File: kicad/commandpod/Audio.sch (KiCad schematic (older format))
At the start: 10 parts

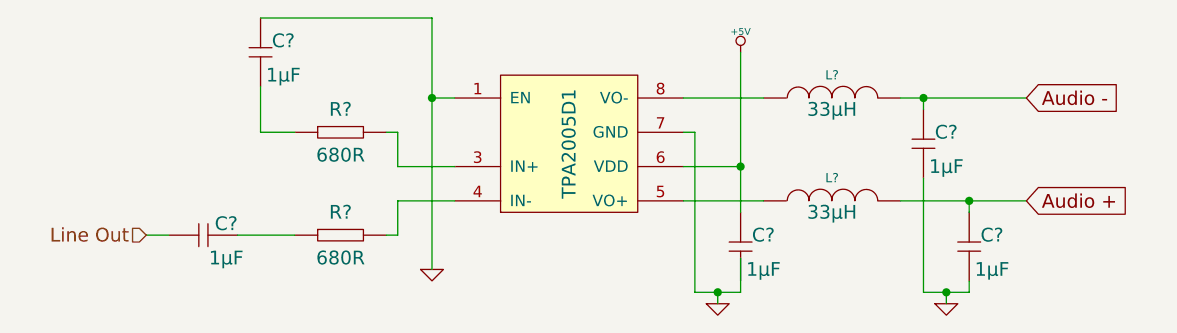
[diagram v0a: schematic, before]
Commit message: Annotated schematics
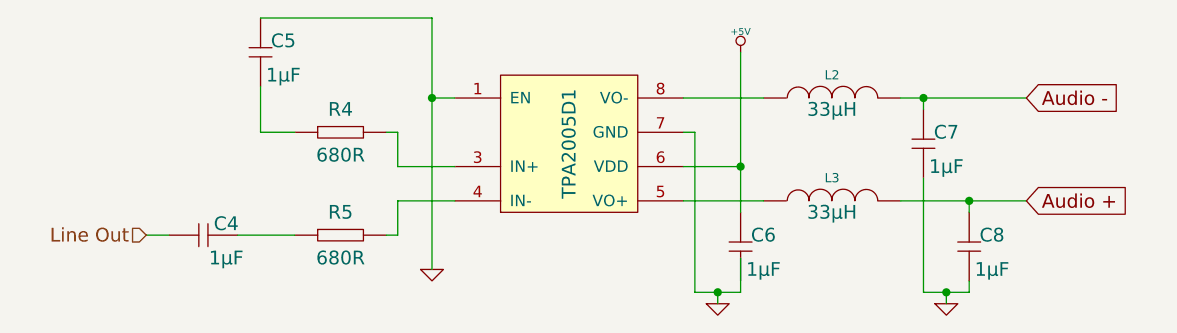
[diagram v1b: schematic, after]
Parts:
- gave numbers to parts that had none: 10
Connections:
- wire segments 36 -> 30
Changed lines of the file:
@@
 $EndDescr
 $Comp
-L TPA2005D1 AMP?
+L TPA2005D1 AMP1
 U 1 1 56D7C1D5
 P 5300 3600
-F 0 "AMP?" H 5100 3250 60  0001 C CNN
+F 0 "AMP1" H 5100 3250 60  0001 C CNN
 F 1 "TPA2005D1" V 5300 3600 60  0000 C CNN
 F 2 "" H 5250 3550 60  0000 C CNN
@@
 Audio -
 $Comp
-L +5V #PWR?
+L +5V #PWR010
 U 1 1 56D7C1DD
 P 6050 3200
-F 0 "#PWR?" H 6050 3290 20  0001 C CNN
+F 0 "#PWR010" H 6050 3290 20  0001 C CNN
 F 1 "+5V" H 6050 3290 30  0000 C CNN
 F 2 "" H 6050 3200 60  0000 C CNN
@@
 $EndComp
 $Comp
-L GND #PWR?
+L GND #PWR011
 U 1 1 56D7C1E3
 P 5950 4300
-F 0 "#PWR?" H 5950 4300 30  0001 C CNN
+F 0 "#PWR011" H 5950 4300 30  0001 C CNN
 F 1 "GND" H 5950 4230 30  0001 C CNN
 F 2 "" H 5950 4300 60  0000 C CNN
@@
 $EndComp
 $Comp
-L INDUCTOR L?
+L INDUCTOR L2
 U 1 1 56D7C1EA
 P 6450 3400
-F 0 "L?" V 6550 3400 40  0000 C CNN
+F 0 "L2" V 6550 3400 40  0000 C CNN
 F 1 "INDUCTOR" V 6550 3400 40  0001 C CNN
 F 2 "~" H 6450 3400 60  0000 C CNN
@@
 $EndComp
 $Comp
-L INDUCTOR L?
+L INDUCTOR L3
 U 1 1 56D7C1F1
 P 6450 3850
-F 0 "L?" V 6550 3850 40  0000 C CNN
+F 0 "L3" V 6550 3850 40  0000 C CNN
 F 1 "INDUCTOR" V 6550 3850 40  0001 C CNN
 F 2 "~" H 6450 3850 60  0000 C CNN
@@
 $EndComp
 $Comp
-L GENERIC_CAPACITOR C?
+L GENERIC_CAPACITOR C7
 U 1 1 56D7C1F9
 P 6850 3600
-F 0 "C?" V 6900 3500 60  0000 C CNN
+F 0 "C7" V 6900 3500 60  0000 C CNN
 F 1 "GENERIC_CAPACITOR" H 6860 3400 60  0001 C CNN
 F 2 "~" H 6820 3350 60  0000 C CNN
@@
 $EndComp
 $Comp
-L GENERIC_CAPACITOR C?
+L GENERIC_CAPACITOR C8
 U 1 1 56D7C201
 P 7050 4050
-F 0 "C?" V 7100 3950 60  0000 C CNN
+F 0 "C8" V 7100 3950 60  0000 C CNN
 F 1 "GENERIC_CAPACITOR" H 7060 3850 60  0001 C CNN
 F 2 "~" H 7020 3800 60  0000 C CNN
@@
 	5800 3850 6150 3850
 Wire Wire Line
-	5800 3700 6050 3700
-Wire Wire Line
-	6750 3400 6850 3400
-Wire Wire Line
-	6850 3400 7300 3400
-Wire Wire Line
 	6850 3400 6850 3450
 Connection ~ 6850 3400
 Wire Wire Line
-	6750 3850 7050 3850
-Wire Wire Line
-	7050 3850 7300 3850
+	6750 3850 7300 3850
 Wire Wire Line
 	7050 3900 7050 3850
 Connection ~ 7050 3850
 $Comp
-L GND #PWR?
+L GND #PWR012
 U 1 1 56D7C212
 P 6950 4300
-F 0 "#PWR?" H 6950 4300 30  0001 C CNN
+F 0 "#PWR012" H 6950 4300 30  0001 C CNN
 F 1 "GND" H 6950 4230 30  0001 C CNN
 F 2 "" H 6950 4300 60  0000 C CNN
@@
 	6850 3750 6850 4250
 Wire Wire Line
-	6850 4250 6950 4250
-Wire Wire Line
-	6950 4250 7050 4250
+	6850 4250 7050 4250
 Wire Wire Line
 	6950 4250 6950 4300
@@
 Connection ~ 6950 4250
 $Comp
-L GENERIC_RESISTOR R?
+L GENERIC_RESISTOR R4
 U 1 1 56D7C220
 P 4300 3550
-F 0 "R?" H 4300 3650 60  0000 C CNN
+F 0 "R4" H 4300 3650 60  0000 C CNN
 F 1 "GENERIC_RESISTOR" H 4340 3330 60  0001 C CNN
 F 2 "~" H 4250 3300 60  0000 C CNN
@@
 $EndComp
 $Comp
-L GENERIC_RESISTOR R?
+L GENERIC_RESISTOR R5
 U 1 1 56D7C228
 P 4300 4000
-F 0 "R?" H 4300 4100 60  0000 C CNN
+F 0 "R5" H 4300 4100 60  0000 C CNN
 F 1 "GENERIC_RESISTOR" H 4340 3780 60  0001 C CNN
 F 2 "~" H 4250 3750 60  0000 C CNN
@@
 $EndComp
 $Comp
-L GND #PWR?
+L GND #PWR013
 U 1 1 56D7C22E
 P 4700 4150
-F 0 "#PWR?" H 4700 4150 30  0001 C CNN
+F 0 "#PWR013" H 4700 4150 30  0001 C CNN
 F 1 "GND" H 4700 4080 30  0001 C CNN
 F 2 "" H 4700 4150 60  0000 C CNN
@@
 $EndComp
 Wire Wire Line
-	4700 3050 4700 3400
-Wire Wire Line
-	4700 3400 4700 4150
+	4700 3050 4700 4150
 Wire Wire Line
 	4700 3400 4800 3400
@@
 	4550 3850 4800 3850
 $Comp
-L GENERIC_CAPACITOR C?
+L GENERIC_CAPACITOR C5
 U 1 1 56D7C23F
 P 3950 3200
-F 0 "C?" V 4000 3100 60  0000 C CNN
+F 0 "C5" V 4000 3100 60  0000 C CNN
 F 1 "GENERIC_CAPACITOR" H 3960 3000 60  0001 C CNN
 F 2 "~" H 3920 2950 60  0000 C CNN
@@
 $EndComp
 $Comp
-L GENERIC_CAPACITOR C?
+L GENERIC_CAPACITOR C4
 U 1 1 56D7C247
 P 3700 4000
-F 0 "C?" H 3800 4050 60  0000 C CNN
+F 0 "C4" H 3800 4050 60  0000 C CNN
 F 1 "GENERIC_CAPACITOR" H 3710 3800 60  0001 C CNN
 F 2 "~" H 3670 3750 60  0000 C CNN
@@
 	3450 4000 3550 4000
 $Comp
-L GENERIC_CAPACITOR C?
+L GENERIC_CAPACITOR C6
 U 1 1 56D7C25B
 P 6050 4050
-F 0 "C?" V 6100 3950 60  0000 C CNN
+F 0 "C6" V 6100 3950 60  0000 C CNN
 F 1 "GENERIC_CAPACITOR" H 6060 3850 60  0001 C CNN
 F 2 "~" H 6020 3800 60  0000 C CNN
@@
 $EndComp
 Wire Wire Line
-	6050 3200 6050 3700
-Wire Wire Line
-	6050 3700 6050 3900
+	6050 3200 6050 3900
 Connection ~ 6050 3700
 Wire Wire Line
-	6050 4100 6050 4250
-Wire Wire Line
-	6050 4250 5950 4250
-Wire Wire Line
-	5950 4250 5850 4250
+	6050 4250 6050 4100
+Wire Wire Line
+	5850 4250 6050 4250
 Wire Wire Line
 	5950 4250 5950 4300
@@
 Text HLabel 3450 4000 0    60   Input ~ 0
 Line Out
+Wire Wire Line
+	5800 3700 6050 3700
+Wire Wire Line
+	6750 3400 7300 3400
 $EndSCHEMATC
